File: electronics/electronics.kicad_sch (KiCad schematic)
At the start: 11 parts, among them J1 USB_C_Receptacle_USB2.0_16P, U1 ESP32-C6-WROOM-1, U2 LM3940IMP-3.3

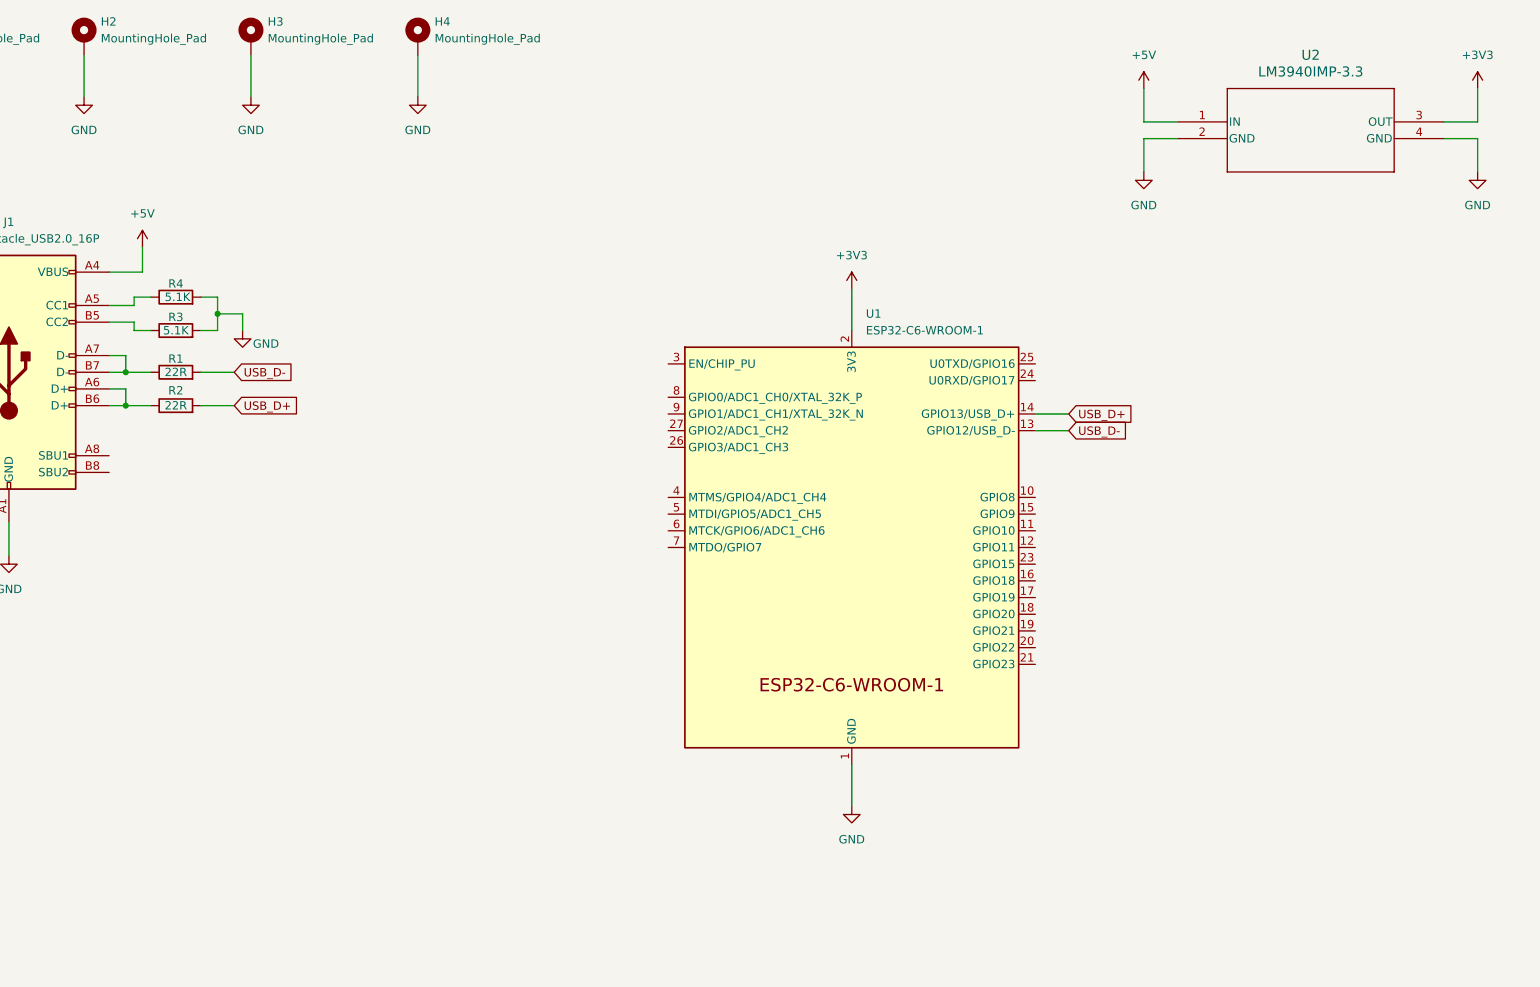
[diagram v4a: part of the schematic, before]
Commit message: pcb: add am2320
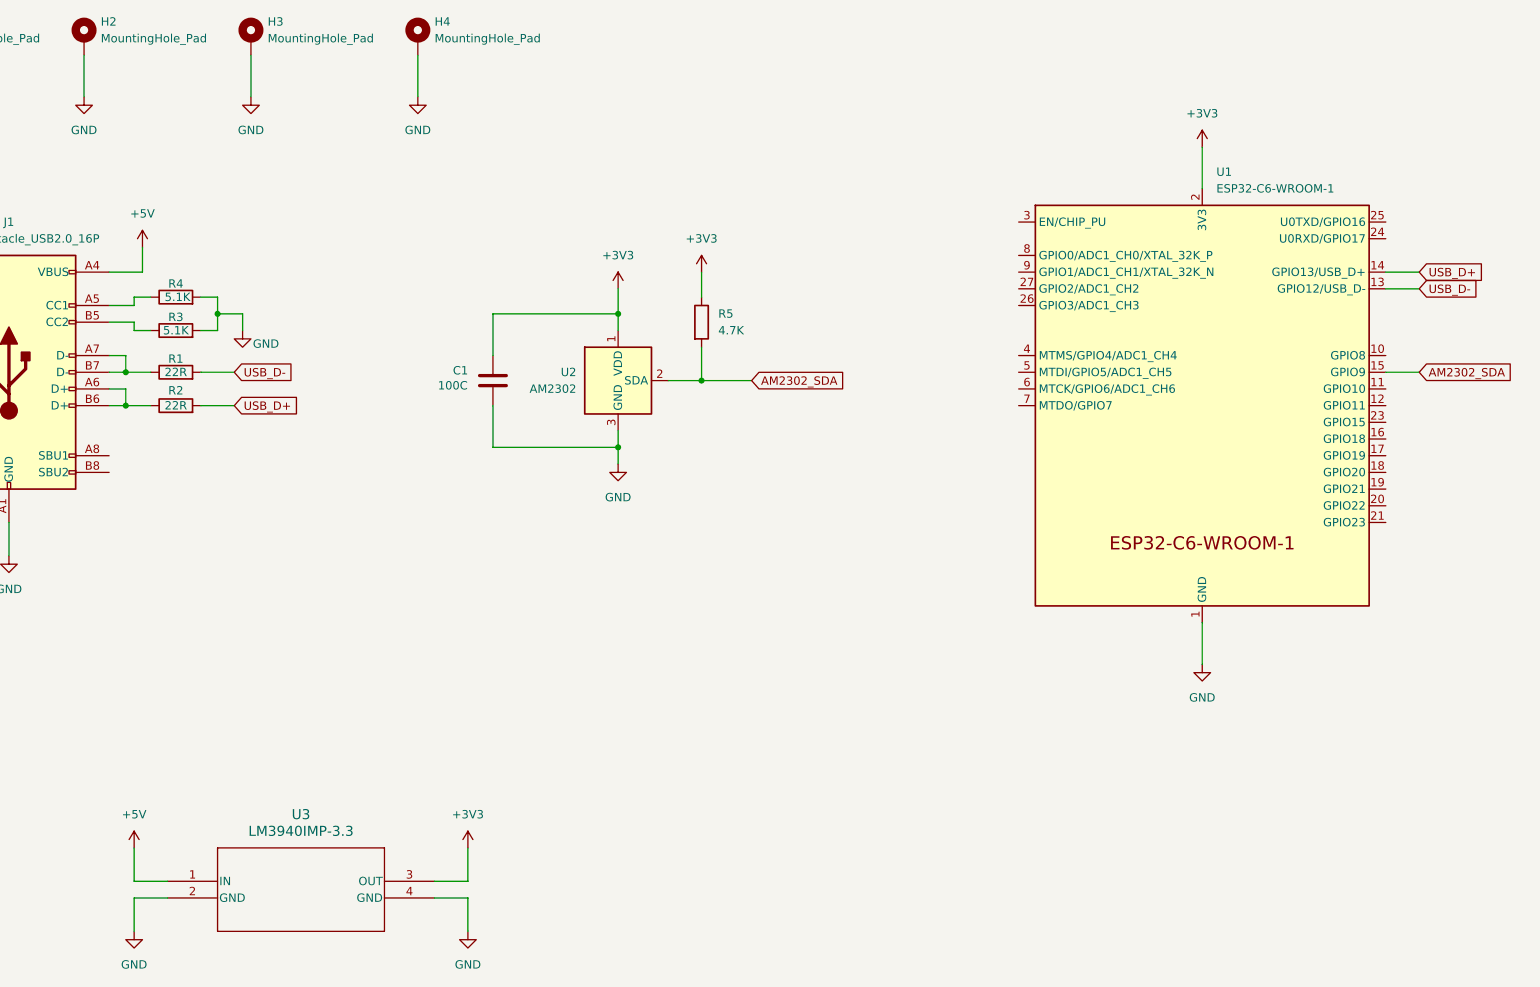
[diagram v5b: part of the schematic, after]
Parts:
- removed U2: LM3940IMP-3.3, footprints:MP04A, symbol Symbols:LM3940IMP-3.3
- added C1: 100C, Capacitor_SMD:C_0805_2012Metric_Pad1.18x1.45mm_HandSolder, symbol Device:C
- added R5: 4.7K, Resistor_SMD:R_0805_2012Metric_Pad1.20x1.40mm_HandSolder, symbol Device:R
- added U2: AM2302, Sensor:ASAIR_AM2302_P2.54mm_Lead2.75mm_TabDown, symbol Sensor:AM2302
- added U3: LM3940IMP-3.3, MP04A, symbol 2025-09-15_16-29-17:LM3940IMP-3.3
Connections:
- net +3V3: now also C1.1, R5.1, U2.1 (VDD), U3.3 (OUT)
- net +5V: now also U3.1 (IN)
- net GND: now also C1.2, U2.3 (GND), U2.4 (GND), U3.2 (GND), U3.4 (GND)
- net AM2302_SDA: now reaches U1.15 (GPIO9)
- net AM2302_SDA: now also R5.2, U2.2 (SDA)
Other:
- moved on the sheet: U1

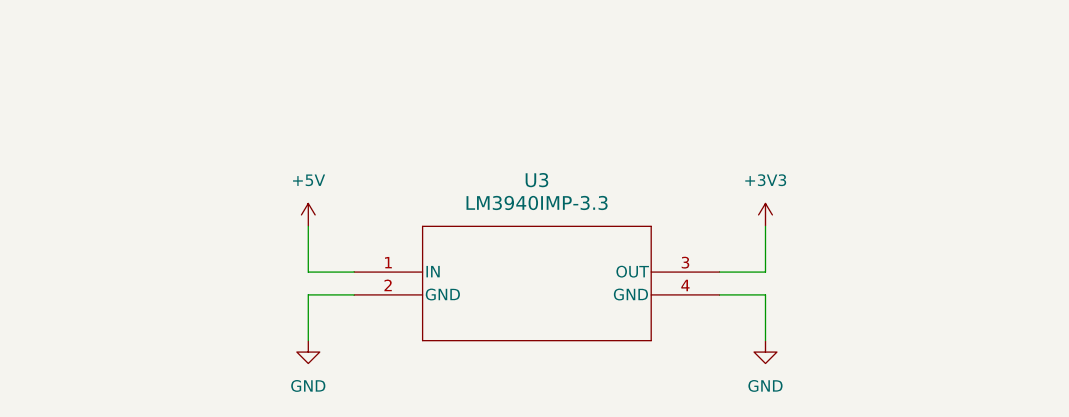
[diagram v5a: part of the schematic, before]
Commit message: schematic: add decoupling caps to regulator
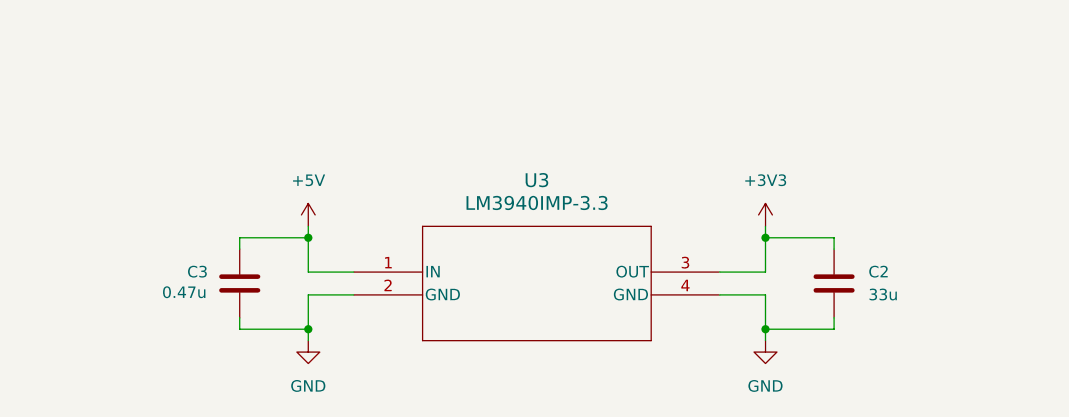
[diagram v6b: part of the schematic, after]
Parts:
- added C2: 33u, symbol Device:C
- added C3: 0.47u, symbol Device:C
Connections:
- net +3V3: now also C2.1
- net +5V: now also C3.1
- net GND: now also C2.2, C3.2

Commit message: schematic: remade schematic
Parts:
- removed R3, R4: 5.1K, Resistor_SMD:R_0805_2012Metric_Pad1.20x1.40mm_HandSolder, symbol Device:R
- removed U2: AM2302, Sensor:ASAIR_AM2302_P2.54mm_Lead2.75mm_TabDown, symbol Sensor:AM2302
- added C4: 0.1u, symbol Device:C
- added C5: 1u, Capacitor_SMD:C_0805_2012Metric_Pad1.18x1.45mm_HandSolder, symbol Device:C
- added R6, R7: 10k, Resistor_SMD:R_0805_2012Metric_Pad1.20x1.40mm_HandSolder, symbol Device:R
- added SW_BOOT, SW_RST: SW_SPST, symbol Switch:SW_SPST
- C1: value 100C -> 22u; footprint Capacitor_SMD:C_0805_2012Metric_Pad1.18x1.45mm_HandSolder -> (none)
- R1, R2: value 22R -> 5.1k; footprint Resistor_SMD:R_0805_2012Metric_Pad1.20x1.40mm_HandSolder -> (none)
- R5: value 4.7K -> 10k
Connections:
- net +3V3: now also C4.1, R6.1, R7.1
- net GND: now also R1.2, R2.1, C4.2, C5.2, SW_BOOT.1 (A), SW_RST.1 (A)
- net USB_D+: now also J1.A6 (D+), J1.B6 (D+); no longer R2.2
- net USB_D-: now also J1.A7 (D-), J1.B7 (D-); no longer R1.2
- net USB_CC1: now reaches J1.A5 (CC1)
- net USB_CC1: now also R1.1
- net USB_CC2: now reaches J1.B5 (CC2)
- net USB_CC2: now also R2.2
- net GPIO8: now reaches U1.10 (GPIO8)
- net GPIO8: now also R6.2
- net EN: now reaches U1.3 (EN/CHIP_PU)
- net EN: now also R5.2, C5.1, SW_RST.2 (B)
- net GPIO0: now reaches U1.8 (GPIO0/ADC1_CH0/XTAL_32K_P)
- net AM2302_SDA renamed GPIO9
- net GPIO9: now also R7.2, SW_BOOT.2 (B); no longer R5.2
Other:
- note added: "BOOT CONFIGURATION"
- note added: "POWER SUPPLY"
- note added: "RESET"
- note added: "USB CONFIGURATION"
- note added: "USB CONNECTOR"
- moved on the sheet: C2, C3, H3, H4, J1, U1, U3
